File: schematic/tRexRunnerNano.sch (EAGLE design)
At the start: 33 parts, among them IC1 MEGA88, IC2 MAX1555, T1 BC857, T2 BC847, T3 BC847, U1 TPS73033DDCR

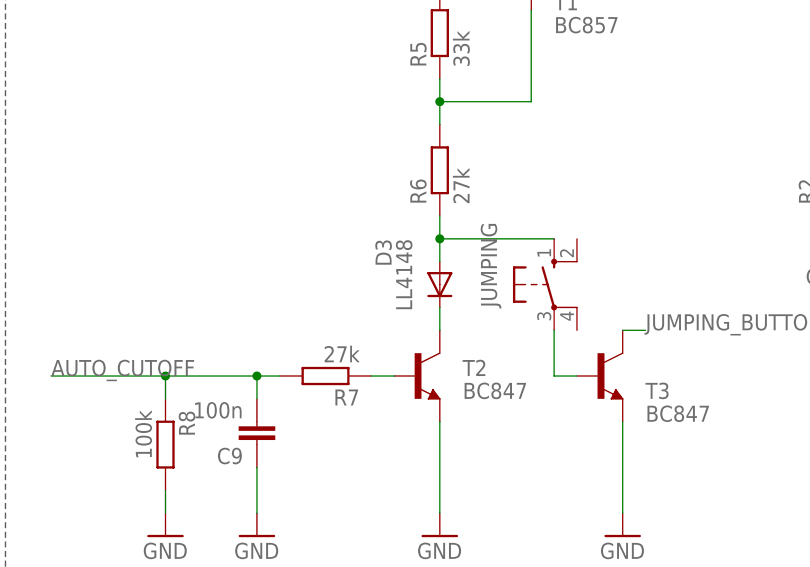
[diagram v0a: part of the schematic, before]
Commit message: Schematic: Changes D3 to 2V7
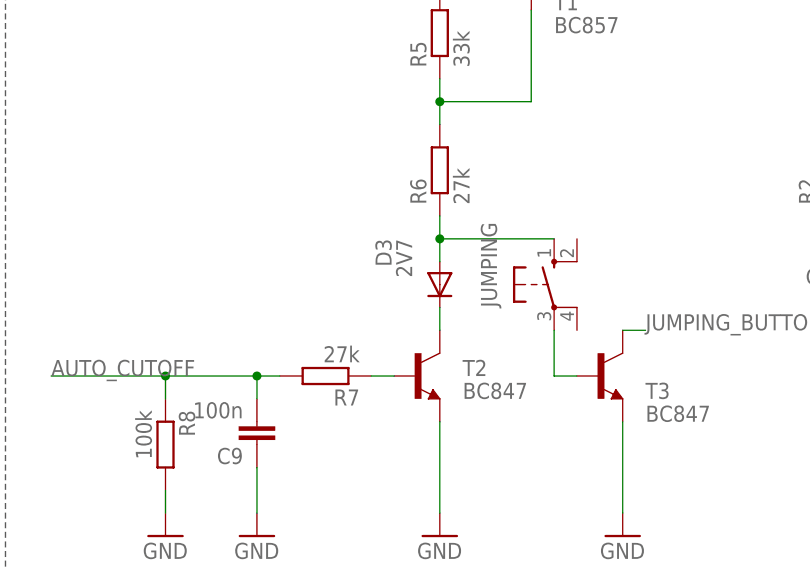
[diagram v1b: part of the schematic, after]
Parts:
- D3: value LL4148 -> 2V7
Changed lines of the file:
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@@
 <part name="GND20" library="supply1" library_urn="urn:adsk.eagle:library:371" deviceset="GND" device=""/>
 <part name="GND21" library="supply1" library_urn="urn:adsk.eagle:library:371" deviceset="GND" device=""/>
-<part name="D3" library="diode" library_urn="urn:adsk.eagle:library:210" deviceset="DIODE-" device="SOD80C" package3d_urn="urn:adsk.eagle:package:43405/2" value="LL4148"/>
+<part name="D3" library="diode" library_urn="urn:adsk.eagle:library:210" deviceset="DIODE-" device="SOD80C" package3d_urn="urn:adsk.eagle:package:43405/2" value="2V7"/>
 <part name="JUMPING" library="switch-omron" library_urn="urn:adsk.eagle:library:377" deviceset="10-XX" device="" package3d_urn="urn:adsk.eagle:package:27496/1"/>
 <part name="DUCKING" library="switch-omron" library_urn="urn:adsk.eagle:library:377" deviceset="10-XX" device="" package3d_urn="urn:adsk.eagle:package:27496/1"/>
